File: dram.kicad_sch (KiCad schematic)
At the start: 8 parts, among them K10 74LS08, U1 74LS280, U2 74LS00, U3 74LS109, U4 74LS04

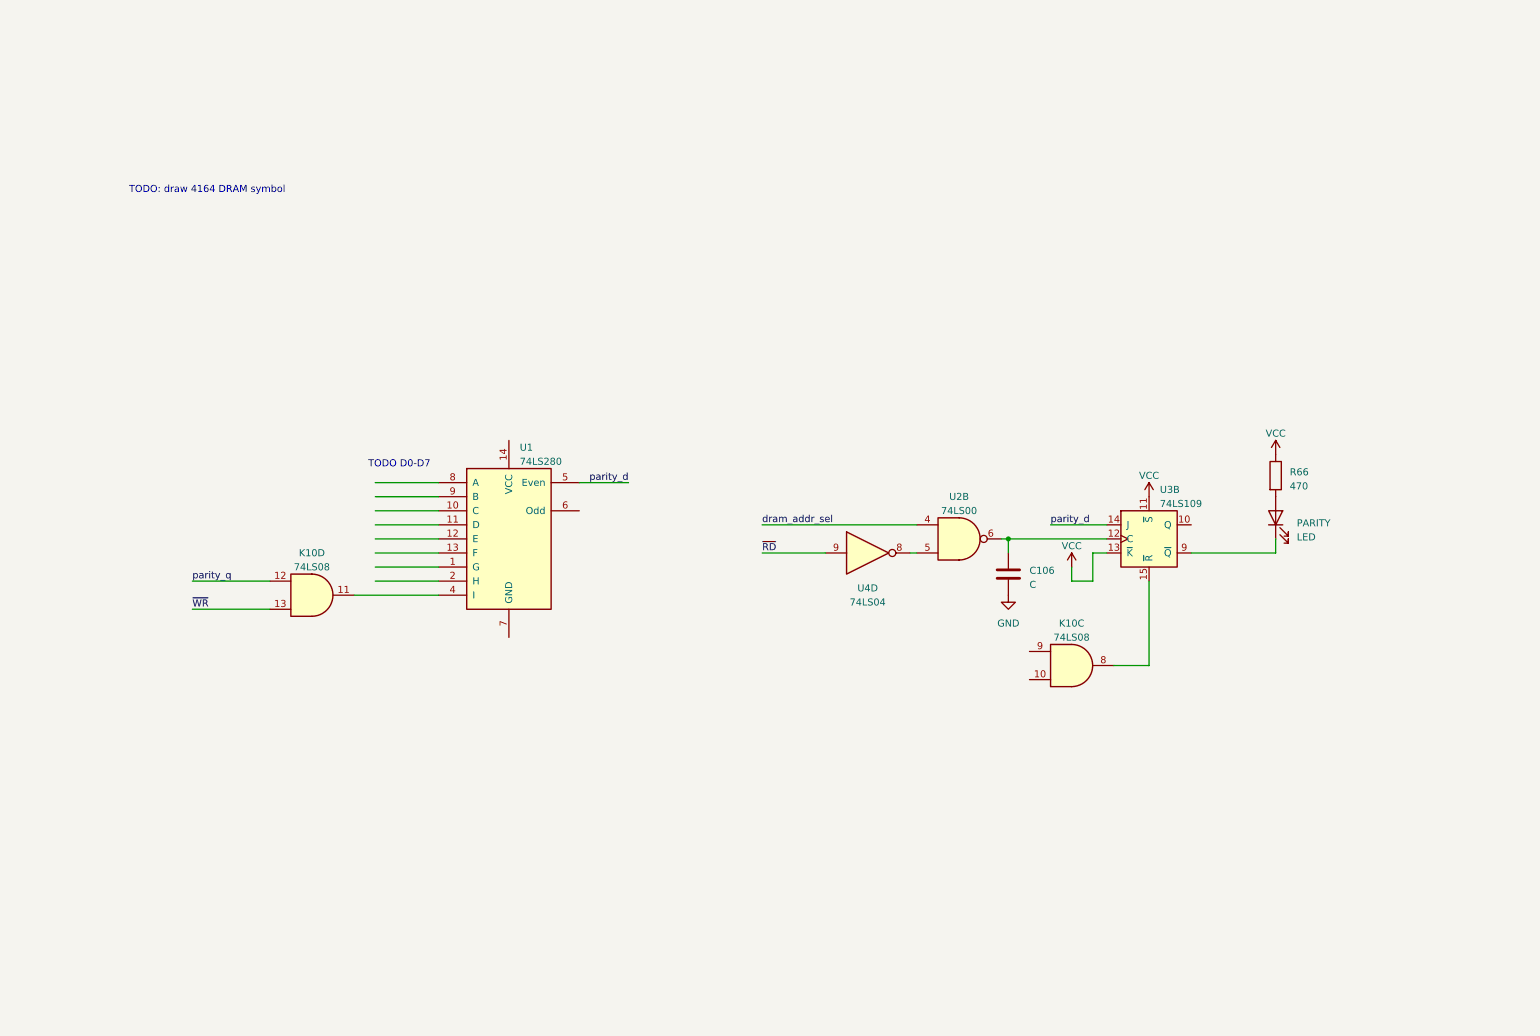
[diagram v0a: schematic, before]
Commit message: DRAM: row/column mux, parity generator (partial), memory ICs
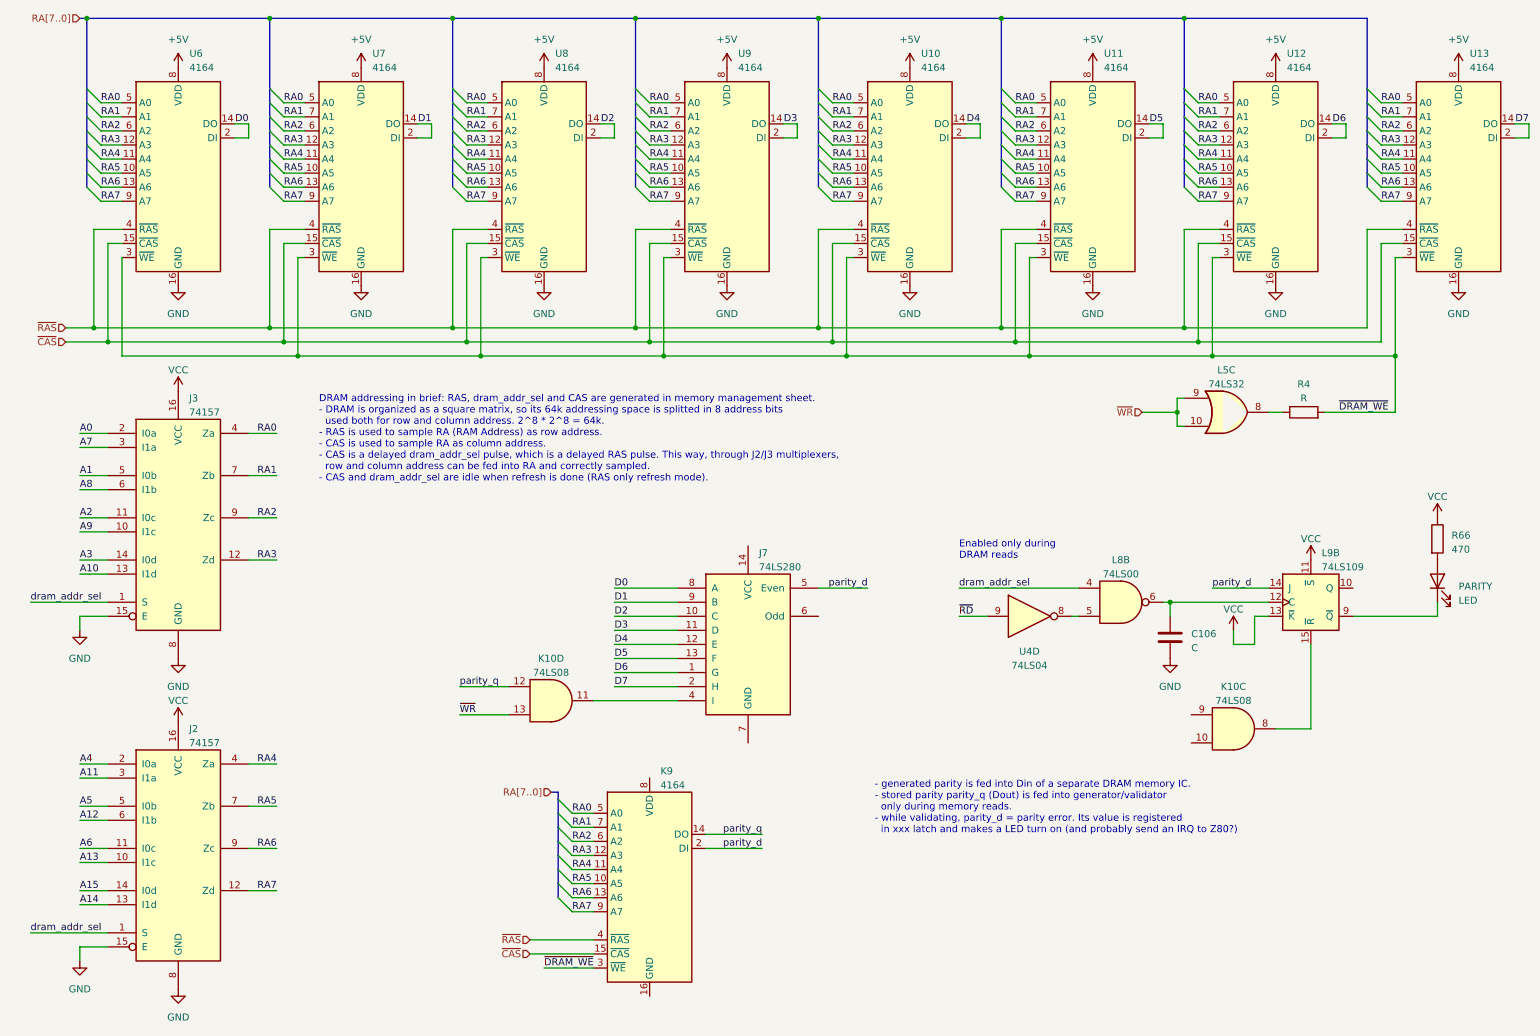
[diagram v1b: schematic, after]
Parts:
- added J2, J3: 74157, symbol 74xx:74LS157
- added K9, U10, U11, U12, U13, U6, U7, U8, U9: 4164, Package_DIP:DIP-16_W7.62mm_LongPads, symbol Vintage:4164
- added L5: 74LS32, symbol 74xx:74LS32
- added R4: R, symbol Device:R
- renumbered U1 to J7, U2 to L8, U3 to L9
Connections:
- net GND: now also J2.15 (E), J2.8 (GND), J3.15 (E), J3.8 (GND), U10.16 (GND), U11.16 (GND), U12.16 (GND), U13.16 (GND), U6.16 (GND), U7.16 (GND), U8.16 (GND), U9.16 (GND)
- net VCC: now also J2.16 (VCC), J3.16 (VCC)
- net dram_addr_sel: now also J2.1 (S), J3.1 (S)
- net parity_d: now also K9.2 (DI)
- net parity_q: now also K9.14 (DO)
- net ~{WR}: now also L5.10, L5.9
- net D6: now reaches J7.1 (G)
- net D6: now also U12.14 (DO), U12.2 (DI)
- net D2: now reaches J7.10 (C)
- net D2: now also U8.14 (DO), U8.2 (DI)
- net D3: now reaches J7.11 (D)
- net D3: now also U9.14 (DO), U9.2 (DI)
- net D4: now reaches J7.12 (E)
- net D4: now also U10.14 (DO), U10.2 (DI)
- net D5: now reaches J7.13 (F)
- net D5: now also U11.14 (DO), U11.2 (DI)
- net D7: now reaches J7.2 (H)
- net D7: now also U13.14 (DO), U13.2 (DI)
- net D0: now reaches J7.8 (A)
- net D0: now also U6.14 (DO), U6.2 (DI)
- net D1: now reaches J7.9 (B)
- net D1: now also U7.14 (DO), U7.2 (DI)
- new net: L5.8, R4.1
- new net +5V: U10.8 (VDD), U11.8 (VDD), U12.8 (VDD), U13.8 (VDD), U6.8 (VDD), U7.8 (VDD), U8.8 (VDD), U9.8 (VDD)
- new net A0: J3.2 (I0a)
- new net A1: J3.5 (I0b)
- new net A10: J3.13 (I1d)
- new net A11: J2.3 (I1a)
- new net A12: J2.6 (I1b)
- new net A13: J2.10 (I1c)
- new net A14: J2.13 (I1d)
- new net A15: J2.14 (I0d)
- new net A2: J3.11 (I0c)
- new net A3: J3.14 (I0d)
- new net A4: J2.2 (I0a)
- new net A5: J2.5 (I0b)
- new net A6: J2.11 (I0c)
- new net A7: J3.3 (I1a)
- new net A8: J3.6 (I1b)
- new net A9: J3.10 (I1c)
- new net RA0: J3.4 (Za), K9.5 (A0), U10.5 (A0), U11.5 (A0), U12.5 (A0), U13.5 (A0), U6.5 (A0), U7.5 (A0), U8.5 (A0), U9.5 (A0)
- new net RA1: J3.7 (Zb), K9.7 (A1), U10.7 (A1), U11.7 (A1), U12.7 (A1), U13.7 (A1), U6.7 (A1), U7.7 (A1), U8.7 (A1), U9.7 (A1)
- new net RA2: J3.9 (Zc), K9.6 (A2), U10.6 (A2), U11.6 (A2), U12.6 (A2), U13.6 (A2), U6.6 (A2), U7.6 (A2), U8.6 (A2), U9.6 (A2)
- new net RA3: J3.12 (Zd), K9.12 (A3), U10.12 (A3), U11.12 (A3), U12.12 (A3), U13.12 (A3), U6.12 (A3), U7.12 (A3), U8.12 (A3), U9.12 (A3)
- new net RA4: J2.4 (Za), K9.11 (A4), U10.11 (A4), U11.11 (A4), U12.11 (A4), U13.11 (A4), U6.11 (A4), U7.11 (A4), U8.11 (A4), U9.11 (A4)
- new net RA5: J2.7 (Zb), K9.10 (A5), U10.10 (A5), U11.10 (A5), U12.10 (A5), U13.10 (A5), U6.10 (A5), U7.10 (A5), U8.10 (A5), U9.10 (A5)
- new net RA6: J2.9 (Zc), K9.13 (A6), U10.13 (A6), U11.13 (A6), U12.13 (A6), U13.13 (A6), U6.13 (A6), U7.13 (A6), U8.13 (A6), U9.13 (A6)
- new net RA7: J2.12 (Zd), K9.9 (A7), U10.9 (A7), U11.9 (A7), U12.9 (A7), U13.9 (A7), U6.9 (A7), U7.9 (A7), U8.9 (A7), U9.9 (A7)
- new net ~{CAS}: K9.15 (~{CAS}), U10.15 (~{CAS}), U11.15 (~{CAS}), U12.15 (~{CAS}), U13.15 (~{CAS}), U6.15 (~{CAS}), U7.15 (~{CAS}), U8.15 (~{CAS}), U9.15 (~{CAS})
- new net ~{DRAM_WE}: K9.3 (~{WE}), R4.2, U10.3 (~{WE}), U11.3 (~{WE}), U12.3 (~{WE}), U13.3 (~{WE}), U6.3 (~{WE}), U7.3 (~{WE}), U8.3 (~{WE}), U9.3 (~{WE})
- new net ~{RAS}: K9.4 (~{RAS}), U10.4 (~{RAS}), U11.4 (~{RAS}), U12.4 (~{RAS}), U13.4 (~{RAS}), U6.4 (~{RAS}), U7.4 (~{RAS}), U8.4 (~{RAS}), U9.4 (~{RAS})
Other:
- note added: "- generated parity is fed into Din of a separate DRAM memory IC. - stored parity parity_q (Dout) is fed into generator/validator only during memory reads. - while validating, parity_d = parity error. Its value is registered in xxx latch and makes a LED turn on (and probably send an IRQ to Z80?)"
- note added: "DRAM addressing in brief: RAS, dram_addr_sel and CAS are generated in memory management sheet. - DRAM is organized as a square matrix, so its 64k addressing space is splitted in 8 address bits used both for row and column address. 2^8 * 2^8 = 64k. - RAS is used to sample RA (RAM Address) as row address. - CAS is used to sample RA as column address. - CAS is a delayed dram_addr_sel pulse, which is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"
- note added: "Enabled only during DRAM reads"
- note removed: "TODO D0-D7"
- note removed: "TODO: draw 4164 DRAM symbol"
- moved on the sheet: C106, J7, K10C, K10D, L8B, L9B, PARITY, R66, U4D
